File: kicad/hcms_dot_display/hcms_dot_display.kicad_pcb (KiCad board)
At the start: 2 copper layers, 35.5 x 39.9 mm, 52 parts, among them J1 Conn_01x12, J2 USB_C_Receptacle_USB2.0, J3 Conn_01x12, J4 Conn_01x11_Female, J5 Conn_01x11_Male, J6 Conn_01x12, J7 Conn_01x12, Q1 Q_PMOS_DSG, Q2 Q_PMOS_DSG, Q3 Q_PMOS_DSG, Q4 Q_PMOS_DSG, Q5 Q_PMOS_DSG, Q6 Q_PMOS_DSG, SW1 SW_DIP_x03, U1 ATtiny826-SXX, U2 FT231XS

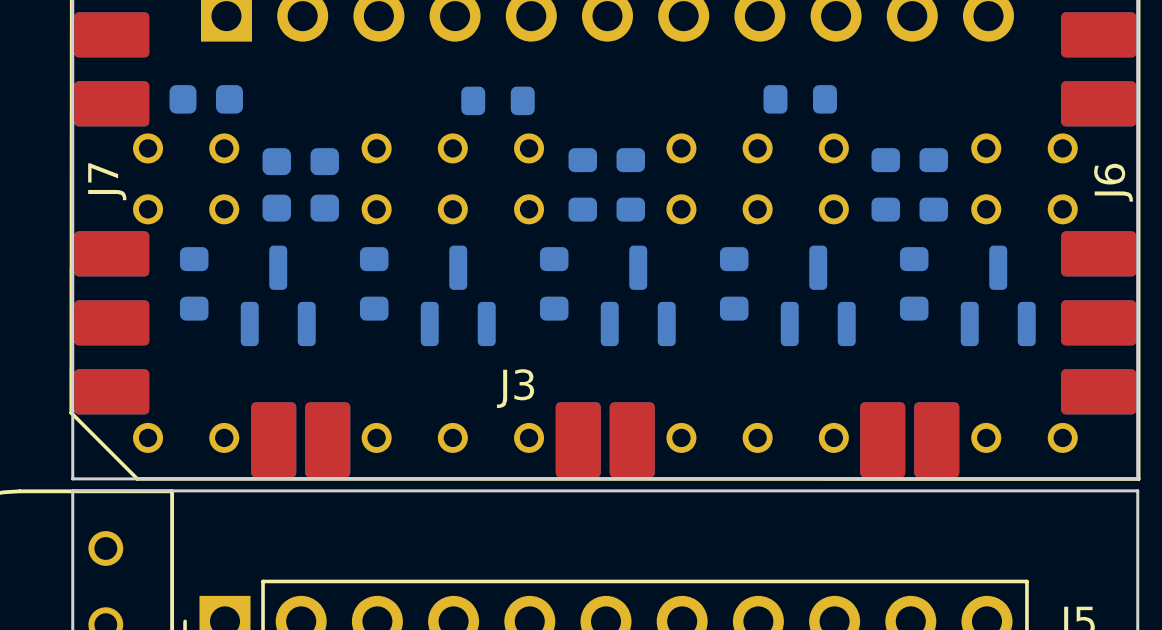
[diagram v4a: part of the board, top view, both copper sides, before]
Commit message: Updated DRC rules to match JLCPCB guide
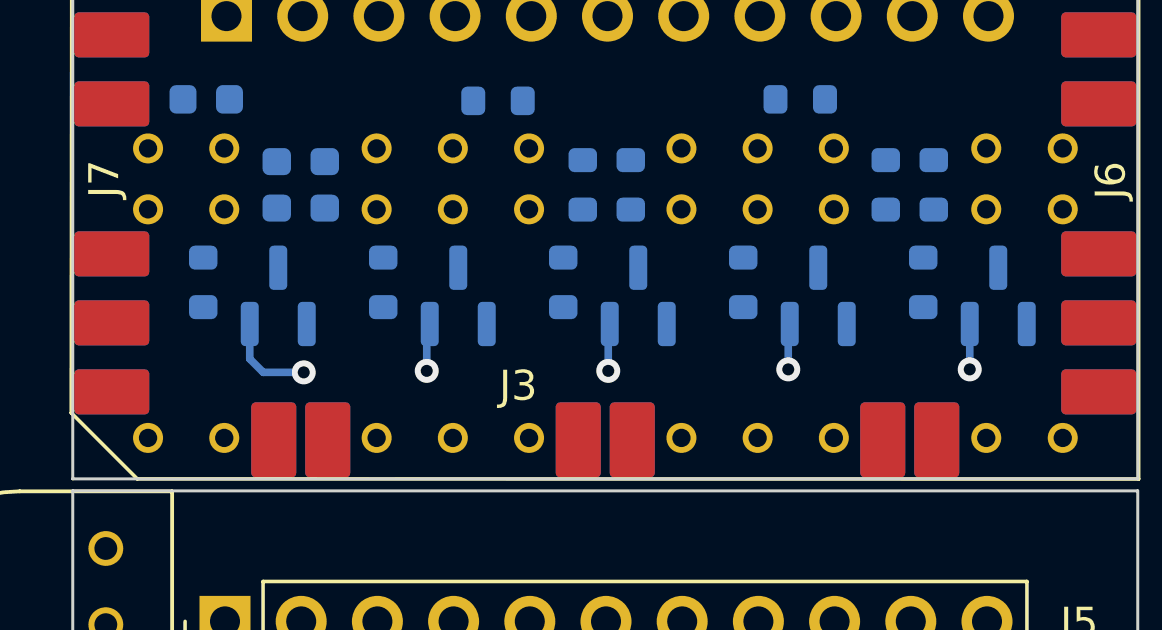
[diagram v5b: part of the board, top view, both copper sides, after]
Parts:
- moved R10 0.30 mm to (179.1, 103.0)
- moved R11 0.30 mm to (167.1, 103.0)
- moved R12 0.30 mm to (185.1, 103.0)
- moved R13 0.30 mm to (173.1, 103.0)
- moved R14 0.30 mm to (191.1, 103.0)
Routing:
- net /V_COL: track 0.00 -> 43.5 mm, vias 0 -> 5
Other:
- copper layers 2 -> 4
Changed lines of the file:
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@@
 (kicad_pcb (version 20211014) (generator pcbnew)
   (general
-    (thickness 1.6)
+    (thickness 4.69)
   )
   (paper "A4")
   (layers
     (0 "F.Cu" signal)
+    (1 "In1.Cu" signal)
+    (2 "In2.Cu" signal)
     (31 "B.Cu" signal)
     (32 "B.Adhes" user "B.Adhesive")
@@
       (layer "F.Cu" (type "copper") (thickness 0.035))
       (layer "dielectric 1" (type "core") (thickness 1.51) (material "FR4") (epsilon_r 4.5) (loss_tangent 0.02))
+      (layer "In1.Cu" (type "copper") (thickness 0.035))
+      (layer "dielectric 2" (type "prepreg") (thickness 1.51) (material "FR4") (epsilon_r 4.5) (loss_tangent 0.02))
+      (layer "In2.Cu" (type "copper") (thickness 0.035))
+      (layer "dielectric 3" (type "core") (thickness 1.51) (material "FR4") (epsilon_r 4.5) (loss_tangent 0.02))
       (layer "B.Cu" (type "copper") (thickness 0.035))
       (layer "B.Mask" (type "Bottom Solder Mask") (thickness 0.01))
@@
   )
   (footprint "Resistor_SMD:R_0603_1608Metric" (layer "B.Cu")
-    (at 172.8 103.1 90)
+    (at 173.1 103.05 90)
     (descr "Resistor SMD 0603 (1608 Metric), square (rectangular) end terminal, IPC_7351 nominal, (Body size source: IPC-SM-782 page 72, https://www.pcb-3d.com/wordpress/wp-content/uploads/ipc-sm-782a_amendment_1_and_2.pdf), generated with kicad-footprint-generator")
     (tags "resistor")
@@
   )
   (footprint "Resistor_SMD:R_0603_1608Metric" (layer "B.Cu")
-    (at 184.8 103.1 90)
+    (at 185.1 103.05 90)
     (descr "Resistor SMD 0603 (1608 Metric), square (rectangular) end terminal, IPC_7351 nominal, (Body size source: IPC-SM-782 page 72, https://www.pcb-3d.com/wordpress/wp-content/uploads/ipc-sm-782a_amendment_1_and_2.pdf), generated with kicad-footprint-generator")
     (tags "resistor")
@@
   )
   (footprint "Resistor_SMD:R_0603_1608Metric" (layer "B.Cu")
-    (at 166.8 103.1 90)
+    (at 167.1 103.05 90)
     (descr "Resistor SMD 0603 (1608 Metric), square (rectangular) end terminal, IPC_7351 nominal, (Body size source: IPC-SM-782 page 72, https://www.pcb-3d.com/wordpress/wp-content/uploads/ipc-sm-782a_amendment_1_and_2.pdf), generated with kicad-footprint-generator")
     (tags "resistor")
@@
   )
   (footprint "Resistor_SMD:R_0603_1608Metric" (layer "B.Cu")
-    (at 178.8 103.1 90)
+    (at 179.1 103.05 90)
     (descr "Resistor SMD 0603 (1608 Metric), square (rectangular) end terminal, IPC_7351 nominal, (Body size source: IPC-SM-782 page 72, https://www.pcb-3d.com/wordpress/wp-content/uploads/ipc-sm-782a_amendment_1_and_2.pdf), generated with kicad-footprint-generator")
     (tags "resistor")
@@
   )
   (footprint "Resistor_SMD:R_0603_1608Metric" (layer "B.Cu")
-    (at 190.8 103.1 90)
+    (at 191.1 103.05 90)
     (descr "Resistor SMD 0603 (1608 Metric), square (rectangular) end terminal, IPC_7351 nominal, (Body size source: IPC-SM-782 page 72, https://www.pcb-3d.com/wordpress/wp-content/uploads/ipc-sm-782a_amendment_1_and_2.pdf), generated with kicad-footprint-generator")
     (tags "resistor")
@@
     (effects (font (size 1 1) (thickness 0.15)) (justify left mirror))
   )
+  (via (at 174.55 106) (size 0.8) (drill 0.4) (layers "F.Cu" "B.Cu") (net 6))
+  (via (at 192.65 105.95) (size 0.8) (drill 0.4) (layers "F.Cu" "B.Cu") (net 6))
+  (via (at 170.45 106.05) (size 0.8) (drill 0.4) (layers "F.Cu" "B.Cu") (net 6))
+  (via (at 186.6 105.95) (size 0.8) (drill 0.4) (layers "F.Cu" "B.Cu") (net 6))
+  (via (at 180.6 106) (size 0.8) (drill 0.4) (layers "F.Cu" "B.Cu") (net 6))
+  (segment (start 170.415 106.015) (end 170.45 106.05) (width 0.254) (layer "In1.Cu") (net 6))
+  (segment (start 170.415001 94.174996) (end 170.415001 106.015003) (width 0.254) (layer "In1.Cu") (net 6))
+  (segment (start 174.55 106) (end 180.6 106) (width 0.254) (layer "In2.Cu") (net 6))
+  (segment (start 186.55 106) (end 186.6 105.95) (width 0.254) (layer "In2.Cu") (net 6))
+  (segment (start 180.6 106) (end 186.55 106) (width 0.254) (layer "In2.Cu") (net 6))
+  (segment (start 174.5 106.05) (end 174.55 106) (width 0.254) (layer "In2.Cu") (net 6))
+  (segment (start 186.6 105.95) (end 192.65 105.95) (width 0.254) (layer "In2.Cu") (net 6))
+  (segment (start 170.450002 106.050004) (end 174.500007 106.050004) (width 0.254) (layer "In2.Cu") (net 6))
+  (segment (start 174.55 106) (end 174.55 104.5375) (width 0.254) (layer "B.Cu") (net 6))
+  (segment (start 180.6 106) (end 180.6 104.4875) (width 0.254) (layer "B.Cu") (net 6))
+  (segment (start 169.1 106.05) (end 168.65 105.6) (width 0.254) (layer "B.Cu") (net 6))
+  (segment (start 180.6 104.4875) (end 180.65 104.4375) (width 0.254) (layer "B.Cu") (net 6))
+  (segment (start 170.45 106.05) (end 169.1 106.05) (width 0.254) (layer "B.Cu") (net 6))
+  (segment (start 186.6 105.95) (end 186.6 104.4875) (width 0.254) (layer "B.Cu") (net 6))
+  (segment (start 174.55 104.5375) (end 174.65 104.4375) (width 0.254) (layer "B.Cu") (net 6))
+  (segment (start 168.65 105.6) (end 168.65 104.4375) (width 0.254) (layer "B.Cu") (net 6))
+  (segment (start 186.6 104.4875) (end 186.65 104.4375) (width 0.254) (layer "B.Cu") (net 6))
+  (segment (start 192.65 105.95) (end 192.65 104.4375) (width 0.254) (layer "B.Cu") (net 6))
 )

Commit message: I did a lot of routing lol
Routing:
- net /CLK: track 0.00 -> 81.9 mm, vias 0 -> 7
- net /B_DATA: track 0.00 -> 52.9 mm, vias 0 -> 3
- net /A_DATA: track 0.00 -> 45.1 mm, vias 0 -> 4
- net /nBLNK: track 0.00 -> 42.4 mm, vias 0 -> 2
- net /DAISY_B_DATA: track 0.00 -> 37.4 mm, vias 0 -> 6
- net /DAISY_A_DATA: track 0.00 -> 35.0 mm, vias 0 -> 7
- net /V_COL: track 43.5 -> 71.7 mm, vias 5 -> 8
- net Net-(D1-Pad26B): track 0.00 -> 23.0 mm, vias 0 -> 2
- net /MCU_COL_5: track 0.00 -> 16.3 mm, vias 0 -> 2
- net /COL_4: track 0.00 -> 15.7 mm, vias 0 -> 1
- net /COL_2: track 0.00 -> 13.8 mm, vias 0 -> 1
- net /MCU_COL_2: track 0.00 -> 13.0 mm, vias 0 -> 2
- net /MCU_COL_3: track 0.00 -> 12.8 mm, vias 0 -> 2
- net /MCU_COL_4: track 0.00 -> 12.1 mm, vias 0 -> 2
- net /COL_5: track 0.00 -> 11.6 mm, vias 0 -> 1
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
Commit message: moar route
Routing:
- net /MCU_COL_3: track 12.8 -> 67.8 mm, vias 2 -> 8
- net /MCU_COL_2: track 13.0 -> 66.6 mm, vias 2 -> 7
- net /MCU_COL_1: track 10.2 -> 55.9 mm, vias 1 -> 6
- net Net-(D1-Pad26B): track 23.0 -> 23.6 mm

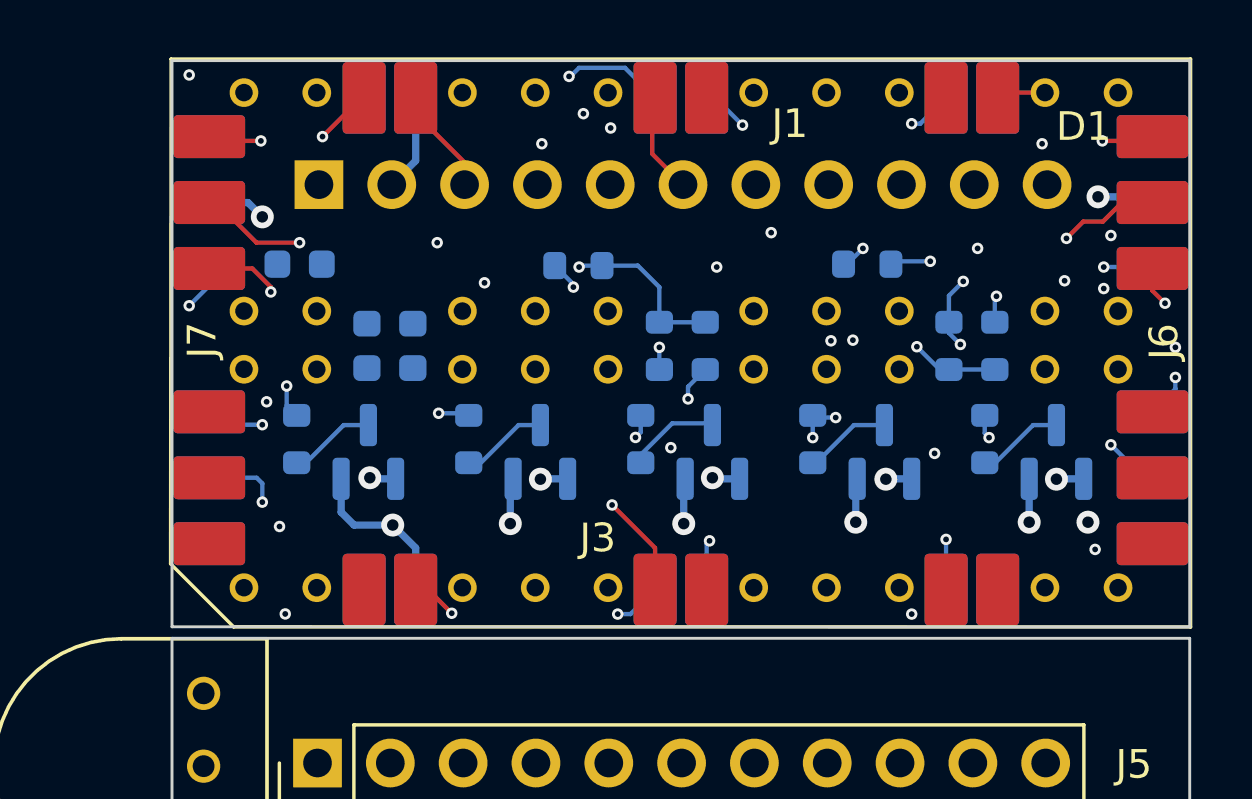
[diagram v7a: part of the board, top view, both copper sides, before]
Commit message: Finished first draft of display board routing
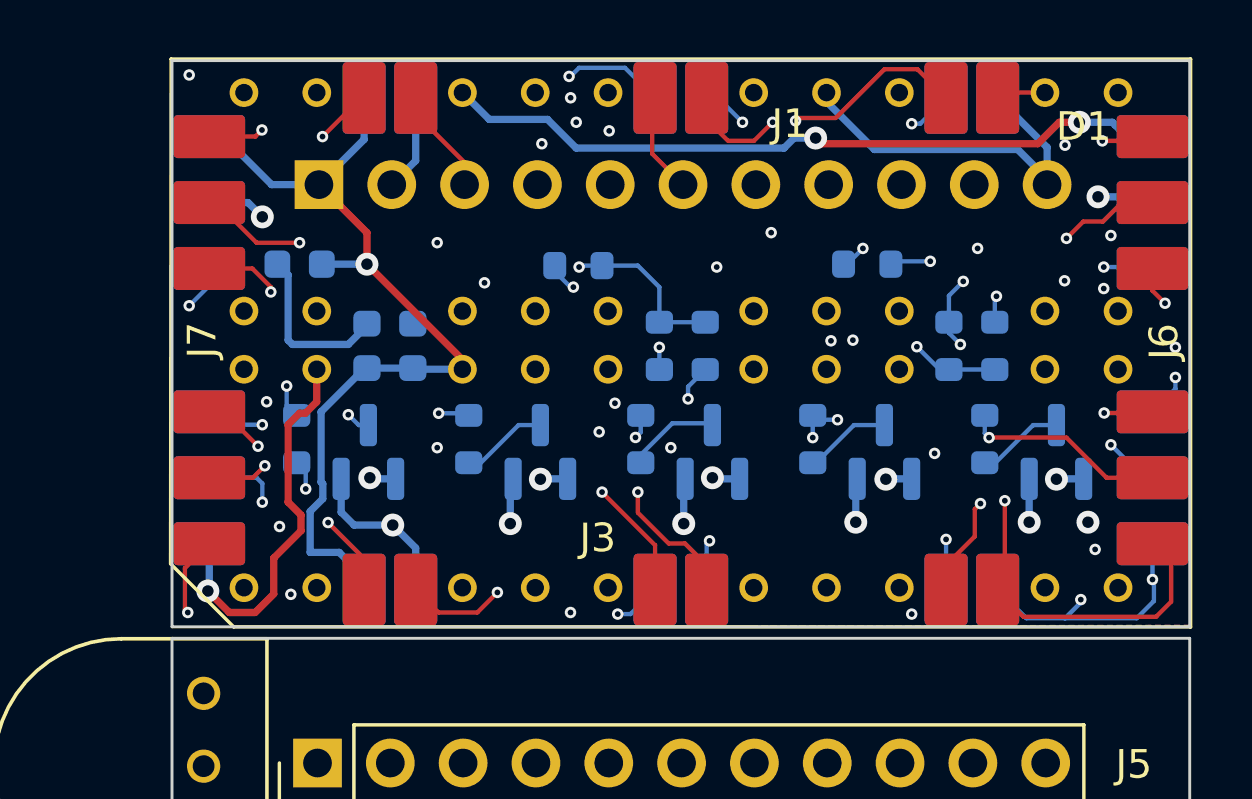
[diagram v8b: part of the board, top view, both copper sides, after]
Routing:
- net +5V: track 0.00 -> 63.6 mm, vias 0 -> 3
- net /MCU_COL_4: track 12.1 -> 71.1 mm, vias 2 -> 9
- net /MCU_COL_5: track 16.3 -> 67.3 mm, vias 2 -> 5
- net /nBLNK: track 42.4 -> 87.9 mm, vias 2 -> 5
- net GND: track 0.00 -> 41.5 mm, vias 0 -> 3
- net Net-(D1-Pad26A): track 9.62 -> 34.3 mm
- net /MCU_COL_1: track 55.9 -> 71.8 mm, vias 6 -> 7
- net /COL_1: track 7.80 -> 12.2 mm
- net /MCU_COL_2: track 66.6 -> 69.9 mm
- net Net-(Q2-Pad3): track 3.04 -> 5.43 mm, vias 0 -> 2
- net /A_DATA: track 45.1 -> 45.9 mm
- net Net-(D1-Pad26B): track 23.6 -> 23.1 mm
- net /MCU_COL_3: track 67.8 -> 68.2 mm, vias 8 -> 9
- added copper zone on B.Cu, net GND
- added copper zone on F.Cu, net GND
- added copper zone on In1.Cu, net GND
- added copper zone on In2.Cu, net GND
